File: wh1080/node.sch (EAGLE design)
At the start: 5 parts, among them J1 AVR_SPI_PRG_62X3_LOCK

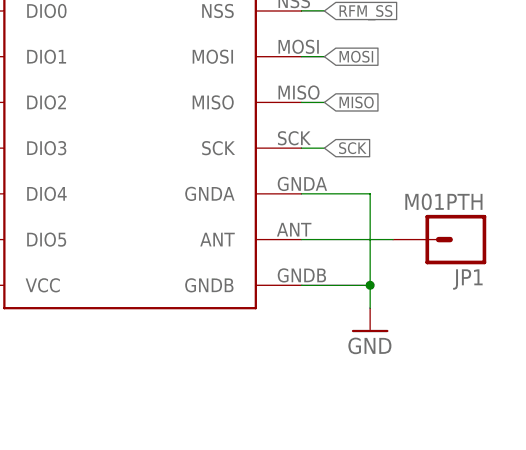
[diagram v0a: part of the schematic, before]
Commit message: routed wh1080 txer
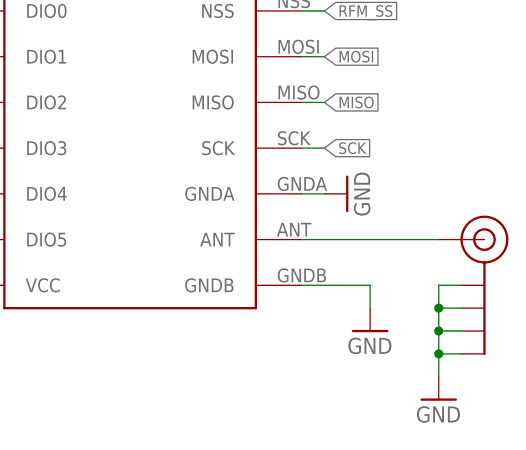
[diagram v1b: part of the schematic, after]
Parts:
- removed JP1: M01PTH, SparkFun-Connectors:M01PTH
- added J$1: SMA_EDGE, jonsowman:SMA_EDGE
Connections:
- removed net N$3: JP1.1, U$4.ANT
- new net N$1: J$1.SIGNAL, U$4.ANT
- net GND: now also J$1.GND@0, J$1.GND@1, J$1.GND@2, J$1.GND@3
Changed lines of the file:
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@@
 <?xml version="1.0" encoding="utf-8"?>
 <!DOCTYPE eagle SYSTEM "eagle.dtd">
-<eagle version="6.5.0">
+<eagle version="6.6.0">
 <drawing>
 <settings>
@@
 <part name="SUPPLY5" library="SparkFun-Aesthetics" deviceset="VCC" device=""/>
 <part name="GND6" library="SparkFun-Aesthetics" deviceset="GND" device=""/>
-<part name="JP1" library="SparkFun-Connectors" deviceset="M01" device="PTH"/>
 <part name="JP2" library="SparkFun-Connectors" deviceset="M03" device="PTH"/>
 <part name="SUPPLY2" library="SparkFun-Aesthetics" deviceset="VCC" device=""/>
 <part name="GND2" library="SparkFun-Aesthetics" deviceset="GND" device=""/>
+<part name="J$1" library="jonsowman" deviceset="SMA_EDGE" device=""/>
+<part name="GND3" library="SparkFun-Aesthetics" deviceset="GND" device=""/>
+<part name="GND5" library="SparkFun-Aesthetics" deviceset="GND" device=""/>
 </parts>
 <sheets>
@@
 <instance part="SUPPLY5" gate="G$1" x="147.32" y="20.32"/>
 <instance part="GND6" gate="1" x="198.12" y="12.7"/>
-<instance part="JP1" gate="G$1" x="208.28" y="22.86" rot="R180"/>
 <instance part="JP2" gate="G$1" x="-22.86" y="22.86"/>
 <instance part="SUPPLY2" gate="G$1" x="-5.08" y="20.32"/>
 <instance part="GND2" gate="1" x="-10.16" y="22.86" rot="R90"/>
+<instance part="J$1" gate="1" x="210.82" y="22.86"/>
+<instance part="GND3" gate="1" x="195.58" y="27.94" rot="R90"/>
+<instance part="GND5" gate="1" x="205.74" y="5.08"/>
 </instances>
 <busses>
@@
 <wire x1="190.5" y1="17.78" x2="198.12" y2="17.78" width="0.1524" layer="91"/>
 <wire x1="198.12" y1="17.78" x2="198.12" y2="15.24" width="0.1524" layer="91"/>
-<pinref part="U$4" gate="A" pin="GNDA"/>
-<wire x1="190.5" y1="27.94" x2="198.12" y2="27.94" width="0.1524" layer="91"/>
-<wire x1="198.12" y1="27.94" x2="198.12" y2="17.78" width="0.1524" layer="91"/>
-<junction x="198.12" y="17.78"/>
 </segment>
 <segment>
@@
 <pinref part="JP2" gate="G$1" pin="2"/>
 <wire x1="-12.7" y1="22.86" x2="-15.24" y2="22.86" width="0.1524" layer="91"/>
+</segment>
+<segment>
+<pinref part="U$4" gate="A" pin="GNDA"/>
+<pinref part="GND3" gate="1" pin="GND"/>
+<wire x1="193.04" y1="27.94" x2="190.5" y2="27.94" width="0.1524" layer="91"/>
+</segment>
+<segment>
+<pinref part="J$1" gate="1" pin="GND@3"/>
+<pinref part="GND5" gate="1" pin="GND"/>
+<wire x1="208.28" y1="10.16" x2="205.74" y2="10.16" width="0.1524" layer="91"/>
+<wire x1="205.74" y1="10.16" x2="205.74" y2="7.62" width="0.1524" layer="91"/>
+<pinref part="J$1" gate="1" pin="GND@2"/>
+<wire x1="208.28" y1="12.7" x2="205.74" y2="12.7" width="0.1524" layer="91"/>
+<wire x1="205.74" y1="12.7" x2="205.74" y2="10.16" width="0.1524" layer="91"/>
+<junction x="205.74" y="10.16"/>
+<pinref part="J$1" gate="1" pin="GND@1"/>
+<wire x1="208.28" y1="15.24" x2="205.74" y2="15.24" width="0.1524" layer="91"/>
+<wire x1="205.74" y1="15.24" x2="205.74" y2="12.7" width="0.1524" layer="91"/>
+<junction x="205.74" y="12.7"/>
+<pinref part="J$1" gate="1" pin="GND@0"/>
+<wire x1="208.28" y1="17.78" x2="205.74" y2="17.78" width="0.1524" layer="91"/>
+<wire x1="205.74" y1="17.78" x2="205.74" y2="15.24" width="0.1524" layer="91"/>
+<junction x="205.74" y="15.24"/>
 </segment>
 </net>
@@
 </segment>
 </net>
-<net name="N$3" class="0">
-<segment>
-<pinref part="JP1" gate="G$1" pin="1"/>
-<pinref part="U$4" gate="A" pin="ANT"/>
-<wire x1="200.66" y1="22.86" x2="190.5" y2="22.86" width="0.1524" layer="91"/>
-</segment>
-</net>
 <net name="SCK" class="0">
 <segment>
@@
 </segment>
 </net>
+<net name="N$1" class="0">
+<segment>
+<pinref part="J$1" gate="1" pin="SIGNAL"/>
+<pinref part="U$4" gate="A" pin="ANT"/>
+<wire x1="205.74" y1="22.86" x2="190.5" y2="22.86" width="0.1524" layer="91"/>
+</segment>
+</net>
